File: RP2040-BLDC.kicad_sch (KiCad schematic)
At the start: 34 parts, among them J1 Motor, J1 USB_B_Micro, J2 Conn_01x02, J4 Motor power, U2 AS5048A, U3 RP2040, Y1 ABLS-12.000MHZ-B4-T

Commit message: WIP
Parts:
- removed H1, H2, H3, H4: MountingHole, MountingHole:MountingHole_3.2mm_M3, symbol Mechanical:MountingHole
- removed J1: Motor, Connector_JST:JST_XH_B3B-XH-A_1x03_P2.50mm_Vertical, symbol Connector:Conn_01x03_Pin
- removed J4: Motor power, Connector_JST:JST_XH_B2B-XH-A_1x02_P2.50mm_Vertical, symbol Connector_Generic:Conn_01x02
- removed U2: AS5048A, Package_SO:TSSOP-14_4.4x5mm_P0.65mm, symbol Sensor_Magnetic:AS5048A
- removed U3: ~, MyLibrary:WQFN-24_EP_2.93x2.93_Pitch0.4mm, symbol Motor_drivers:DRV8311P
- added D2: MBR1020VL, Diode_SMD:D_SOD-123F, symbol Diode:MBR1020VL
- added J5: MPWR, Connector_PinHeader_2.54mm:PinHeader_1x02_P2.54mm_Vertical, symbol Connector_Generic:Conn_01x02
- added J6: I2C5V, Connector_JST:JST_SH_BM04B-SRSS-TB_1x04-1MP_P1.00mm_Vertical, symbol Connector_Generic:Conn_01x04
- added J6: M1, Connector_JST:JST_XH_S3B-XH-A_1x03_P2.50mm_Horizontal, symbol Connector:Conn_01x03_Pin
- added J7: M2, Connector_JST:JST_XH_S3B-XH-A_1x03_P2.50mm_Horizontal, symbol Connector:Conn_01x03_Pin
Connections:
- net GND: now also J5.1 (Pin_1), J6.4 (Pin_4)
- net VCOM renamed +5V
- net +5V: now also D2.1 (K)
- new net: D2.2 (A), J6.3 (Pin_3)
- new net +BATT: J5.2 (Pin_2)
- new net Driver sensor pair/MA: J6.1 (Pin_1)
- new net Driver sensor pair/MB: J6.2 (Pin_2)
- new net Driver sensor pair/MC: J6.3 (Pin_3)
- new net Driver sensor pair1/MA: J7.1 (Pin_1)
- new net Driver sensor pair1/MB: J7.2 (Pin_2)
- new net Driver sensor pair1/MC: J7.3 (Pin_3)
- new net I2C0_SCL: J6.1 (Pin_1)
- new net I2C0_SDA: J6.2 (Pin_2)
- no-connect marks 3 -> 2
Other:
- added sheet Driver sensor pair (DriverSensor.kicad_sch)
- added sheet Driver sensor pair1 (DriverSensor.kicad_sch)
- note added: "Motor power"
- note added: "To mainboard"
- moved on the sheet: C10, C11, C12, C13, C14, C15, C16, C6, C7, C8, C9, R3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

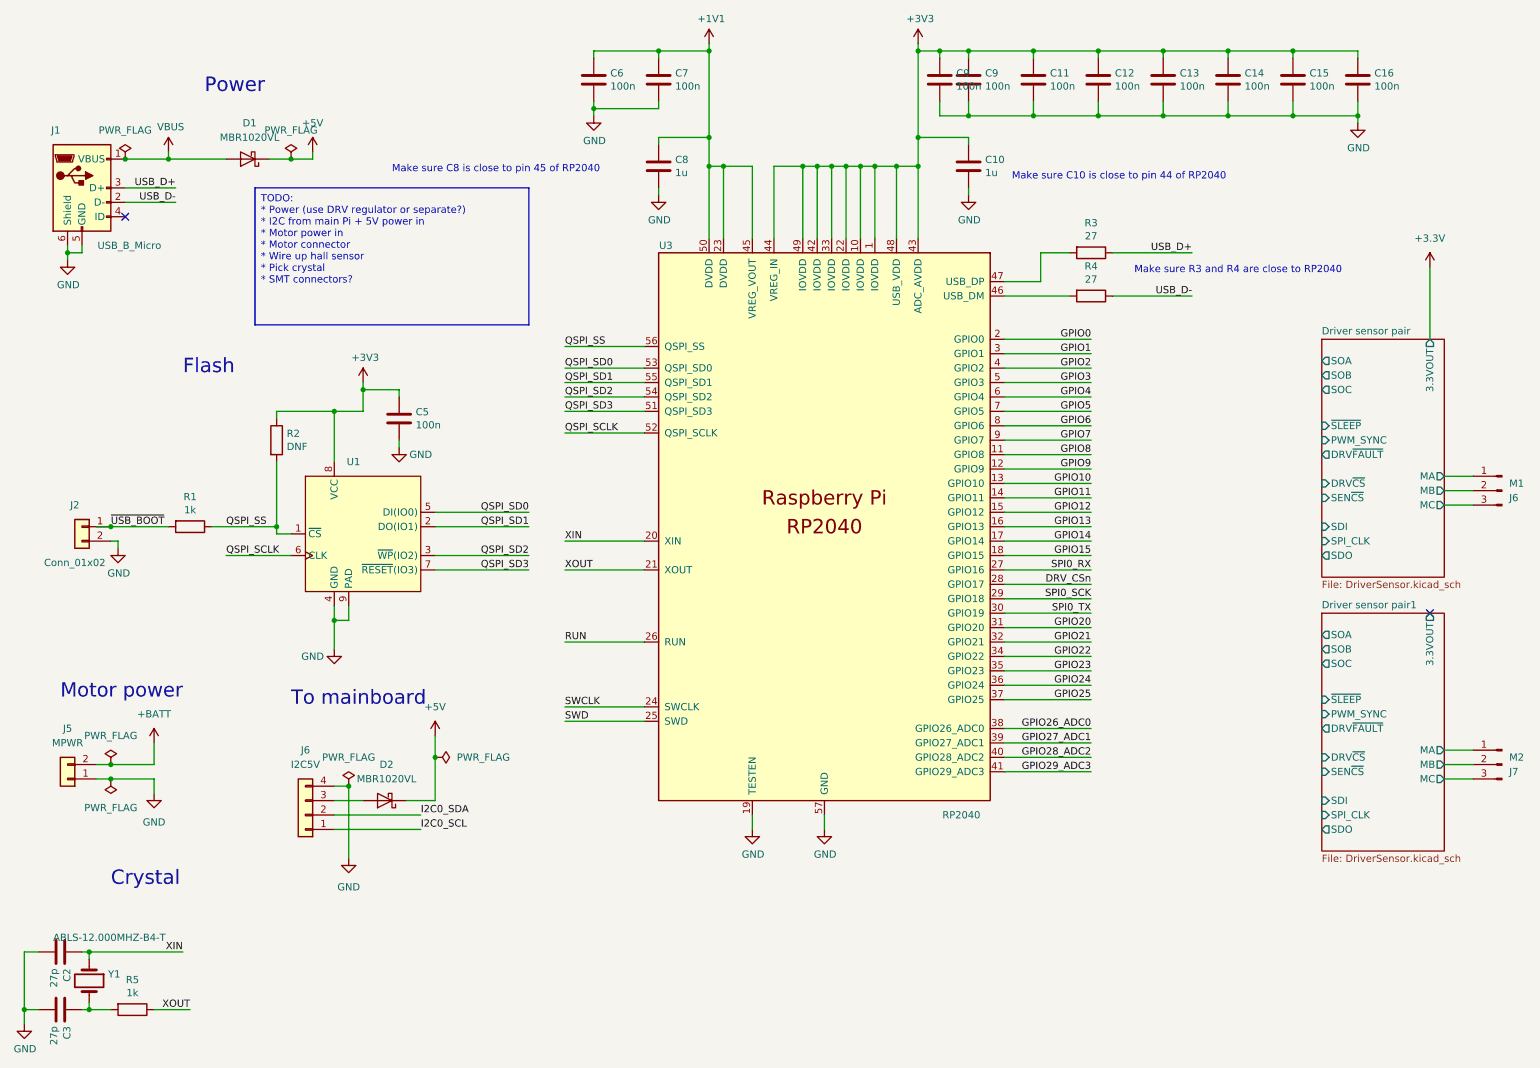
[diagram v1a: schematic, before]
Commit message: First pass at routing board.
- Add INA219 current sensor and shunt
- Route motor traces.
- Still need to fix a few footprints.
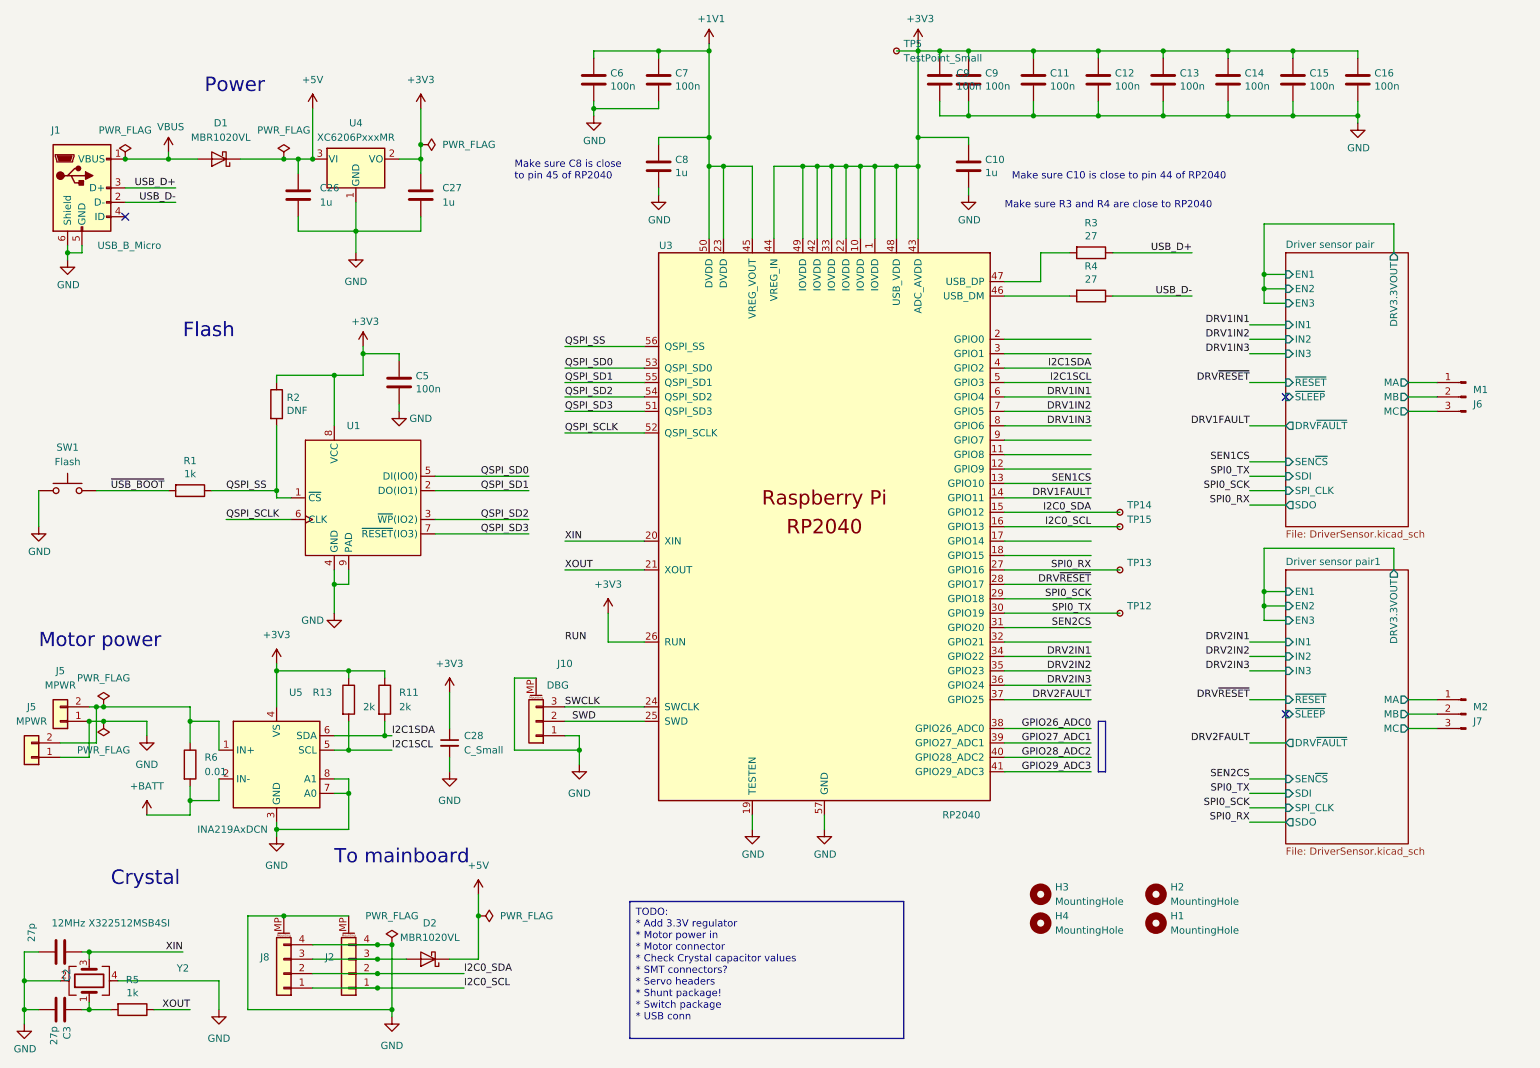
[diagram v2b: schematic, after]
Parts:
- removed J2: Conn_01x02, Connector_PinHeader_2.54mm:PinHeader_1x02_P2.54mm_Vertical, symbol Connector_Generic:Conn_01x02
- removed J6: I2C5V, Connector_JST:JST_SH_BM04B-SRSS-TB_1x04-1MP_P1.00mm_Vertical, symbol Connector_Generic:Conn_01x04
- removed Y1: ABLS-12.000MHZ-B4-T, RP2040_minimal:Crystal_SMD_HC49-US, symbol Device:Crystal
- added C26, C27: 1u, Capacitor_SMD:C_0402_1005Metric, symbol Device:C
- added C28: C_Small, Capacitor_SMD:C_0402_1005Metric, symbol Device:C_Small
- added H1, H2, H3, H4: MountingHole, MountingHole:MountingHole_2.7mm_M2.5, symbol Mechanical:MountingHole
- added J10: DBG, Connector_JST:JST_SH_BM03B-SRSS-TB_1x03-1MP_P1.00mm_Vertical, symbol Connector_Generic_MountingPin:Conn_01x03_MountingPin
- added J2, J8: Conn_01x04_MountingPin, Connector_JST:JST_SH_BM04B-SRSS-TB_1x04-1MP_P1.00mm_Vertical, symbol Connector_Generic_MountingPin:Conn_01x04_MountingPin
- added J5: MPWR, MyLibrary:SolderWire-2.5sqmm_1x02_P7.2mm_D2.4mm_OD3.6mm_ShortRelief, symbol Connector_Generic:Conn_01x02
- added R11, R13: 2k, Resistor_SMD:R_0402_1005Metric, symbol Device:R
- added R6: 0.01, Resistor_SMD:R_1206_3216Metric, symbol Device:R
- added SW1: Flash, Button_Switch_SMD:SW_Push_1P1T_NO_6x6mm_H9.5mm, symbol Switch:SW_Push
- added TP12, TP13, TP14, TP15, TP5: TestPoint_Small, TestPoint:TestPoint_Pad_D1.0mm, symbol Connector:TestPoint_Small
- added U4: XC6206PxxxMR, Package_TO_SOT_SMD:SOT-23-3, symbol Regulator_Linear:XC6206PxxxMR
- added U5: INA219AxDCN, Package_TO_SOT_SMD:SOT-23-8, symbol Sensor_Energy:INA219AxDCN
- added Y2: 12MHz X322512MSB4SI, Crystal:Crystal_SMD_3225-4Pin_3.2x2.5mm, symbol Device:Crystal_GND24
- J5: footprint Connector_PinHeader_2.54mm:PinHeader_1x02_P2.54mm_Vertical -> MyLibrary:SolderWire-2.5sqmm_1x02_P7.2mm_D2.4mm_OD3.6mm_ShortRelief
- J6, J7: footprint Connector_JST:JST_XH_S3B-XH-A_1x03_P2.50mm_Horizontal -> Connector_JST:JST_XH_B3B-XH-A_1x03_P2.50mm_Vertical
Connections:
- net GPIO12 is gone; now on net I2C0_SDA: U3.15 (GPIO12)
- net GPIO13 is gone; now on net I2C0_SCL: U3.16 (GPIO13)
- net +3V3: now also U3.26 (RUN), C27.1, C28.1, R11.1, R13.1, TP5.1, U4.2 (VO), U5.4 (VS)
- net +5V: now also C26.1, U4.3 (VI)
- net +BATT: now also R6.2, U5.2 (IN-); no longer J5.2 (Pin_2)
- net GND: now also C26.2, C27.2, C28.2, J10.1 (Pin_1), J10.MP (MountPin), J2.4 (Pin_4), J2.MP (MountPin), J5.1 (Pin_1), J8.4 (Pin_4), J8.MP (MountPin), SW1.1, U4.1 (GND), U5.3 (GND), U5.7 (A0), U5.8 (A1), Y2.2, Y2.4
- net I2C0_SCL: now also J2.1 (Pin_1), J8.1 (Pin_1), TP15.1
- net I2C0_SDA: now also J2.2 (Pin_2), J8.2 (Pin_2), TP14.1
- net RUN: no longer U3.26 (RUN)
- net SPI0_RX: now also TP13.1
- net SPI0_TX: now also TP12.1
- net SWCLK: now also J10.3 (Pin_3)
- net SWD: now also J10.2 (Pin_2)
- net XIN: now also Y2.3
- net ~{USB_BOOT}: now also SW1.2
- net at D2.2 (A): now also J2.3 (Pin_3), J8.3 (Pin_3)
- net at C3.1, R5.2: now also Y2.1
- net DRV_CSn renamed DRV~{RESET}
- net GPIO0: no longer names the net of U3.2 (GPIO0)
- net GPIO1: no longer names the net of U3.3 (GPIO1)
- net GPIO10 renamed SEN1CS
- net GPIO11 renamed DRV1FAULT
- net GPIO14: no longer names the net of U3.17 (GPIO14)
- net GPIO15: no longer names the net of U3.18 (GPIO15)
- net GPIO2 renamed I2C1SDA
- net I2C1SDA: now also R11.2, U5.6 (SDA)
- net GPIO20 renamed SEN2CS
- net GPIO21: no longer names the net of U3.32 (GPIO21)
- net GPIO22 renamed DRV2IN1
- net GPIO23 renamed DRV2IN2
- net GPIO24 renamed DRV2IN3
- net GPIO25 renamed DRV2FAULT
- net GPIO3 renamed I2C1SCL
- net I2C1SCL: now also R13.2, U5.5 (SCL)
- net GPIO4 renamed DRV1IN1
- net GPIO5 renamed DRV1IN2
- net GPIO6 renamed DRV1IN3
- net GPIO7: no longer names the net of U3.9 (GPIO7)
- net GPIO8: no longer names the net of U3.11 (GPIO8)
- net GPIO9: no longer names the net of U3.12 (GPIO9)
- new net: J5.2 (Pin_2), J5.2 (Pin_2), R6.1, U5.1 (IN+)
- no-connect marks 2 -> 3
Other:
- sheet Driver sensor pair ports: added DRV3.3VOUT, EN1, EN2, EN3, IN1, IN2, IN3, ~{RESET}; removed 3.3VOUT, DRV~{CS}, PWM_SYNC, SOA, SOB, SOC
- sheet Driver sensor pair1 ports: added DRV3.3VOUT, EN1, EN2, EN3, IN1, IN2, IN3, ~{RESET}; removed 3.3VOUT, DRV~{CS}, PWM_SYNC, SOA, SOB, SOC
- moved on the sheet: C5, D1, D2, J5, J6, J7, R1, R2, U1
